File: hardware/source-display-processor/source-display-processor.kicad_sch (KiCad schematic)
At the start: 23 parts, among them J1 conn_br, SW1 SW_Push, U1 MCP23017_SO

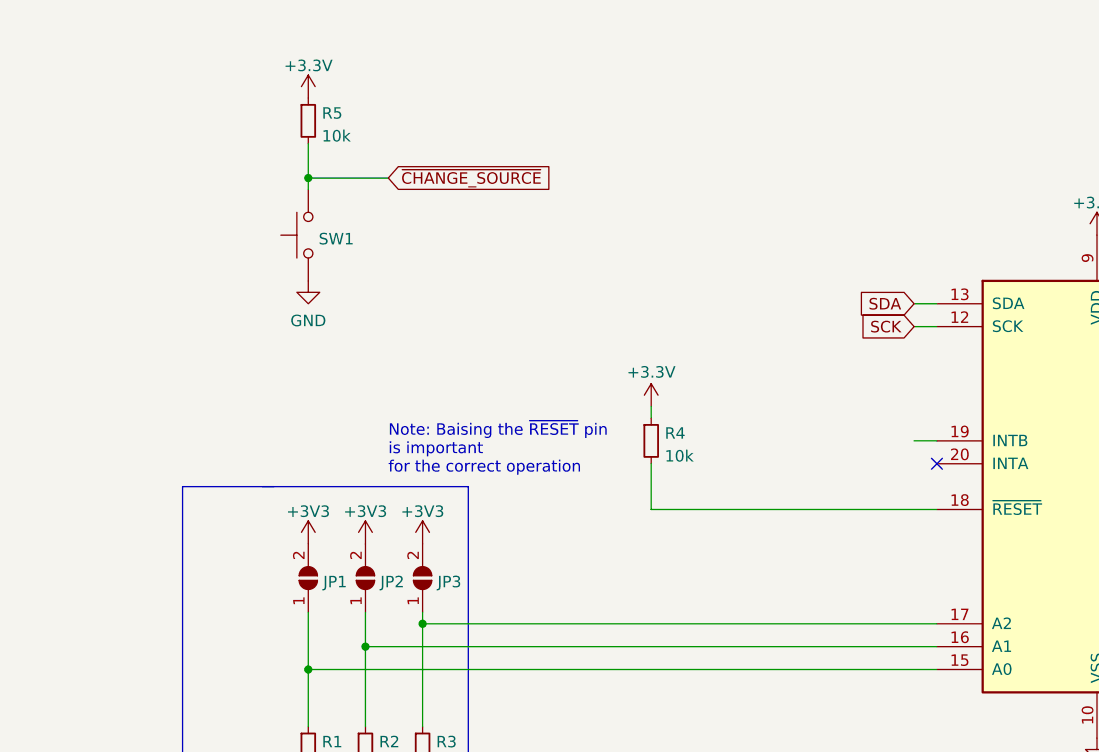
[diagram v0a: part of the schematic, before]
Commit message: Added RC reset circuit
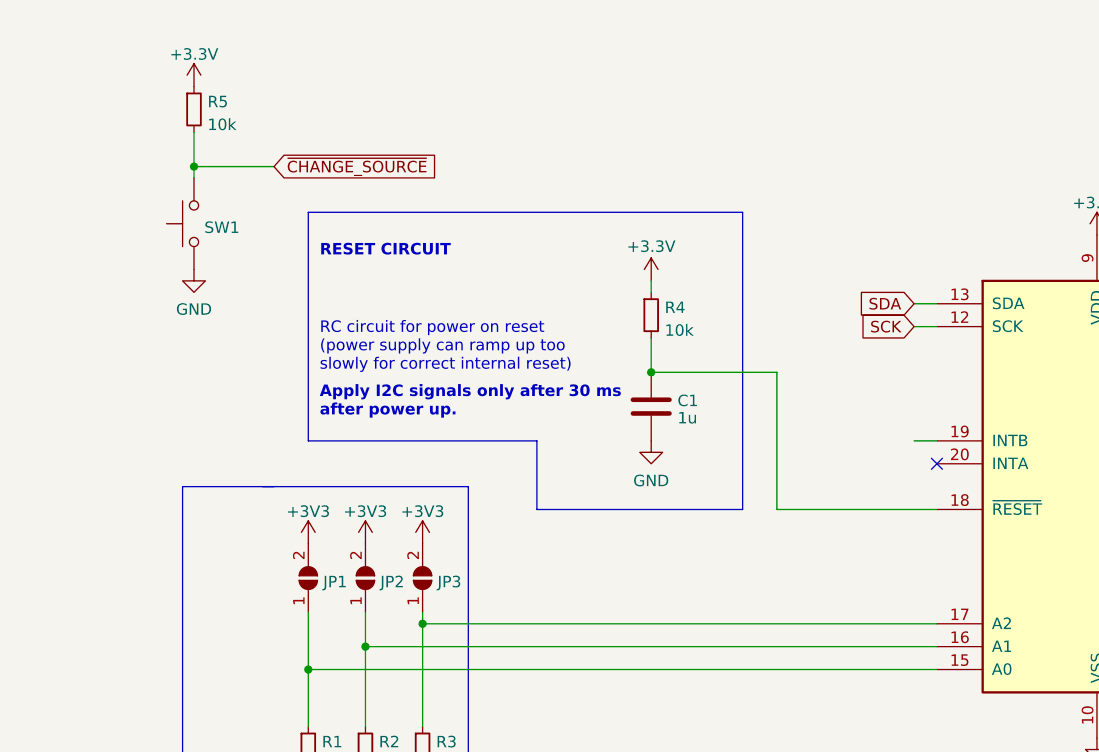
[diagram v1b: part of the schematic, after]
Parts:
- added C1: 1u, symbol Device:C
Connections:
- net GND: now also C1.2
- net at R4.2, U1.18 (~{RESET}): now also C1.1
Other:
- note added: "Apply I2C signals only after 30 ms after power up."
- note added: "RC circuit for power on reset (power supply can ramp up too slowly for correct internal reset)"
- note added: "RESET CIRCUIT"
- note removed: "Note: Baising the ~{RESET} pin is important for the correct operation"
- moved on the sheet: R4, R5, SW1
